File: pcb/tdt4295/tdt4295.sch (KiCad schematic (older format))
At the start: 0 parts

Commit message: simple efm connections
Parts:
- added C?: 1uF, symbol Device:C
- added C? (x2): 12pF, symbol Device:C
- added C?: 4.7uF, symbol Device:C
- added J?: MCU Debug Header, symbol Connector_Generic:Conn_02x10_Odd_Even
- added U?: EFM32GG12B810F1024GQ64, efm32gg-footprint:EFM32GG12B810F1024GQ64, symbol EFM32GG12B810F1024GQ64:EFM32GG12B810F1024GQ64
- added Y?: 48MHz, symbol Device:Crystal_GND24
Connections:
- net labels added: +1V0, +1V8, +3V3, +3V3A, +5V, 48MHZ_P1, 48MHZ_P3, GND, USB_D+, USB_D-
- wire segments 0 -> 88
- no-connect marks 0 -> 6
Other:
- note added: "Vent med å bruke noen av pinnene til QSPI/USART.\nKommer an på hvilke drivere som finnes til EFM-en\nog hva som er enklest i FPGA"

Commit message: Finish labeling/connecting EFM32 pins
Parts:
- added J?: MCU GPIO Header, symbol Connector_Generic:Conn_02x10_Odd_Even
- added J?: SD_Card, symbol Connector:SD_Card
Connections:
- net labels added: DBG_SWCLK, DBG_SWDIO, DBG_SWO, GPIO_PA12, GPIO_PA8, GPIO_PB11, GPIO_PB12, GPIO_PB8, GPIO_PD0, GPIO_PD1, GPIO_PD2, GPIO_PD3, GPIO_PD5, GPIO_PD6, GPIO_PD8, GPIO_PE7, GPIO_PF12, GPIO_PF5, MCU_RESETN, QSPI0_CS0, QSPI0_CS1, QSPI0_DQ0, QSPI0_DQ1, QSPI0_DQ2, QSPI0_DQ3, QSPI0_DQ4, QSPI0_DQ5, QSPI0_DQ6, QSPI0_DQ7, QSPI0_DQS, QSPI0_SCLK, SDIO_CD, SDIO_CLK, SDIO_CMD, SDIO_DAT0, SDIO_DAT1, SDIO_DAT2, SDIO_DAT3, SDIO_WP, US3_CLK, US3_CS, US3_CTS, US3_RTS, US3_RX, US3_TX
- wire segments 88 -> 174
- no-connect marks 6 -> 9
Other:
- note added: "EFM32GG MCU"
- note added: "VREGI/VBUS/VREGO\nAlle knyttet til 5V-regulator\nIkke egt. nødvendig"
- note removed: "Vent med å bruke noen av pinnene til QSPI/USART.\nKommer an på hvilke drivere som finnes til EFM-en\nog hva som er enklest i FPGA"
- moved on the sheet: C?, J?, U?, Y?

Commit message: rework some efm wiring according to application notes
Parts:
- removed C?: 4.7uF, symbol Device:C
- added C? (x5): 0.1uF, symbol Device:C
- added C? (x3): 10uF, symbol Device:C
- added C?: 10nF, symbol Device:C
- added C?: 1uF, symbol Device:C
- added R? (x2): 15, symbol Device:R
- J?: value MCU Debug Header -> ARM 20 Pin Debug Header
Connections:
- wire segments 174 -> 206
- no-connect marks 9 -> 10
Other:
- note added: "AN0046\n2.2"
- note added: "RESETn has internal pullup"
- note added: "See AN0002.1\nFig 3.3"
- note added: "VREGI has\ninternal p.down"
- note removed: "VREGI/VBUS/VREGO\nAlle knyttet til 5V-regulator\nIkke egt. nødvendig"
- moved on the sheet: C?, J?, Y?

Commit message: remove analog 3v3 output
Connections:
- net labels removed: +3V3A
- wire segments 206 -> 204
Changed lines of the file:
@@
 F2 "USB_D+" B R 1900 1050 50
 F3 "USB_D-" B R 1900 1150 50
-F4 "+5V" O R 1900 1450 50
-F5 "+3V3" O R 1900 1550 50
-F6 "+3V3A" O R 1900 1650 50
-F7 "+1V8" O R 1900 1750 50
-F8 "+1V0" O R 1900 1850 50
+F4 "+5V" O R 1900 1550 50
+F5 "+3V3" O R 1900 1650 50
+F6 "+1V8" O R 1900 1750 50
+F7 "+1V0" O R 1900 1850 50
 $EndSheet
 $Comp
@@
 L power:+5V #PWR?
 U 1 1 61455354
-P 2000 1400
-F 0 "#PWR?" H 2000 1250 50  0001 C CNN
-F 1 "+5V" H 2015 1573 50  0000 C CNN
-F 2 "" H 2000 1400 50  0001 C CNN
-F 3 "" H 2000 1400 50  0001 C CNN
-	1    2000 1400
+P 2000 1500
+F 0 "#PWR?" H 2000 1350 50  0001 C CNN
+F 1 "+5V" H 2015 1673 50  0000 C CNN
+F 2 "" H 2000 1500 50  0001 C CNN
+F 3 "" H 2000 1500 50  0001 C CNN
+	1    2000 1500
 	1    0    0    -1
 $EndComp
 Wire Wire Line
-	2000 1400 2000 1450
+	2000 1500 2000 1550
 Wire Wire Line
-	2000 1450 1900 1450
+	2000 1550 1900 1550
 $Comp
 L power:+3V3 #PWR?
 U 1 1 61455D75
-P 2200 1400
-F 0 "#PWR?" H 2200 1250 50  0001 C CNN
-F 1 "+3V3" H 2215 1573 50  0000 C CNN
-F 2 "" H 2200 1400 50  0001 C CNN
-F 3 "" H 2200 1400 50  0001 C CNN
-	1    2200 1400
-	1    0    0    -1
-$EndComp
-$Comp
-L tdt4295:+3V3A #PWR?
-U 1 1 614565B9
-P 2450 1400
-F 0 "#PWR?" H 2450 1250 50  0001 C CNN
-F 1 "+3V3A" H 2465 1573 50  0000 C CNN
-F 2 "" H 2450 1400 50  0001 C CNN
-F 3 "" H 2450 1400 50  0001 C CNN
-	1    2450 1400
+P 2200 1500
+F 0 "#PWR?" H 2200 1350 50  0001 C CNN
+F 1 "+3V3" H 2215 1673 50  0000 C CNN
+F 2 "" H 2200 1500 50  0001 C CNN
+F 3 "" H 2200 1500 50  0001 C CNN
+	1    2200 1500
 	1    0    0    -1
 $EndComp
@@
 L power:+1V8 #PWR?
 U 1 1 61456C3B
-P 2700 1400
-F 0 "#PWR?" H 2700 1250 50  0001 C CNN
-F 1 "+1V8" H 2715 1573 50  0000 C CNN
-F 2 "" H 2700 1400 50  0001 C CNN
-F 3 "" H 2700 1400 50  0001 C CNN
-	1    2700 1400
+P 2450 1500
+F 0 "#PWR?" H 2450 1350 50  0001 C CNN
+F 1 "+1V8" H 2465 1673 50  0000 C CNN
+F 2 "" H 2450 1500 50  0001 C CNN
+F 3 "" H 2450 1500 50  0001 C CNN
+	1    2450 1500
 	1    0    0    -1
 $EndComp
@@
 L power:+1V0 #PWR?
 U 1 1 614570F0
-P 2950 1400
-F 0 "#PWR?" H 2950 1250 50  0001 C CNN
-F 1 "+1V0" H 2965 1573 50  0000 C CNN
-F 2 "" H 2950 1400 50  0001 C CNN
-F 3 "" H 2950 1400 50  0001 C CNN
-	1    2950 1400
+P 2700 1500
+F 0 "#PWR?" H 2700 1350 50  0001 C CNN
+F 1 "+1V0" H 2715 1673 50  0000 C CNN
+F 2 "" H 2700 1500 50  0001 C CNN
+F 3 "" H 2700 1500 50  0001 C CNN
+	1    2700 1500
 	1    0    0    -1
 $EndComp
 Wire Wire Line
-	1900 1550 2200 1550
+	1900 1650 2200 1650
 Wire Wire Line
-	2200 1550 2200 1400
+	2200 1650 2200 1500
 Wire Wire Line
-	2450 1400 2450 1650
+	1900 1750 2450 1750
 Wire Wire Line
-	2450 1650 1900 1650
+	2450 1750 2450 1500
 Wire Wire Line
-	1900 1750 2700 1750
+	2700 1500 2700 1850
 Wire Wire Line
-	2700 1750 2700 1400
-Wire Wire Line
-	2950 1400 2950 1850
-Wire Wire Line
-	2950 1850 1900 1850
+	2700 1850 1900 1850
 $Comp
 L power:GND #PWR?

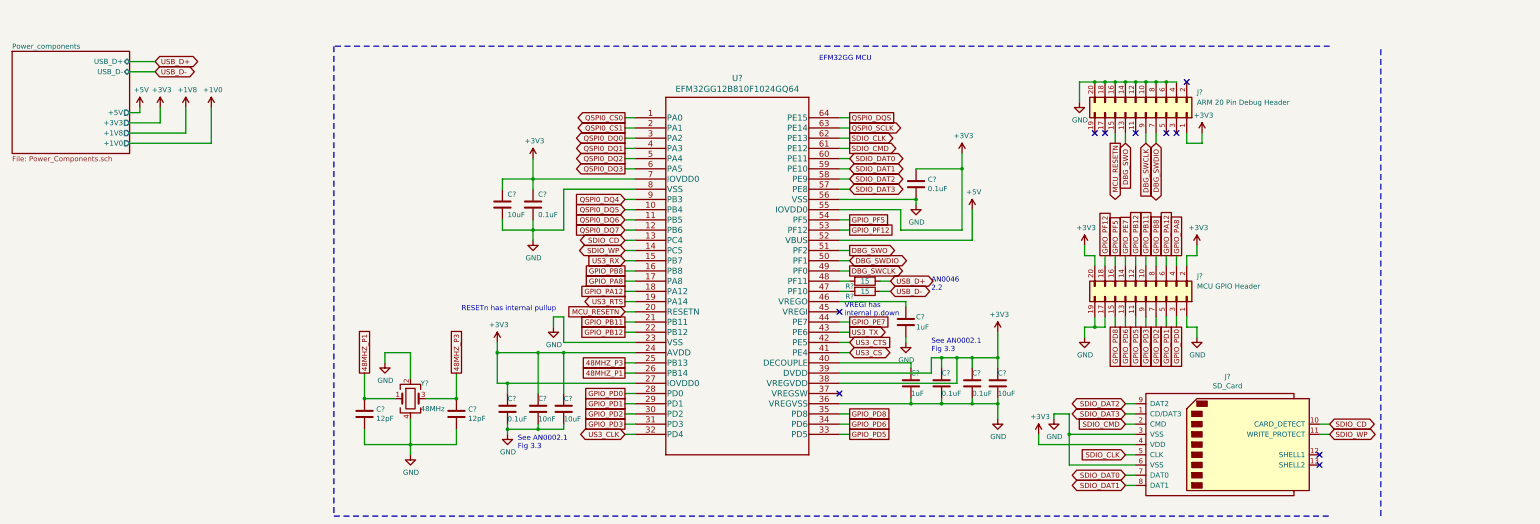
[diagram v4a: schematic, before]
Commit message: rework power regulator to only use tps54294
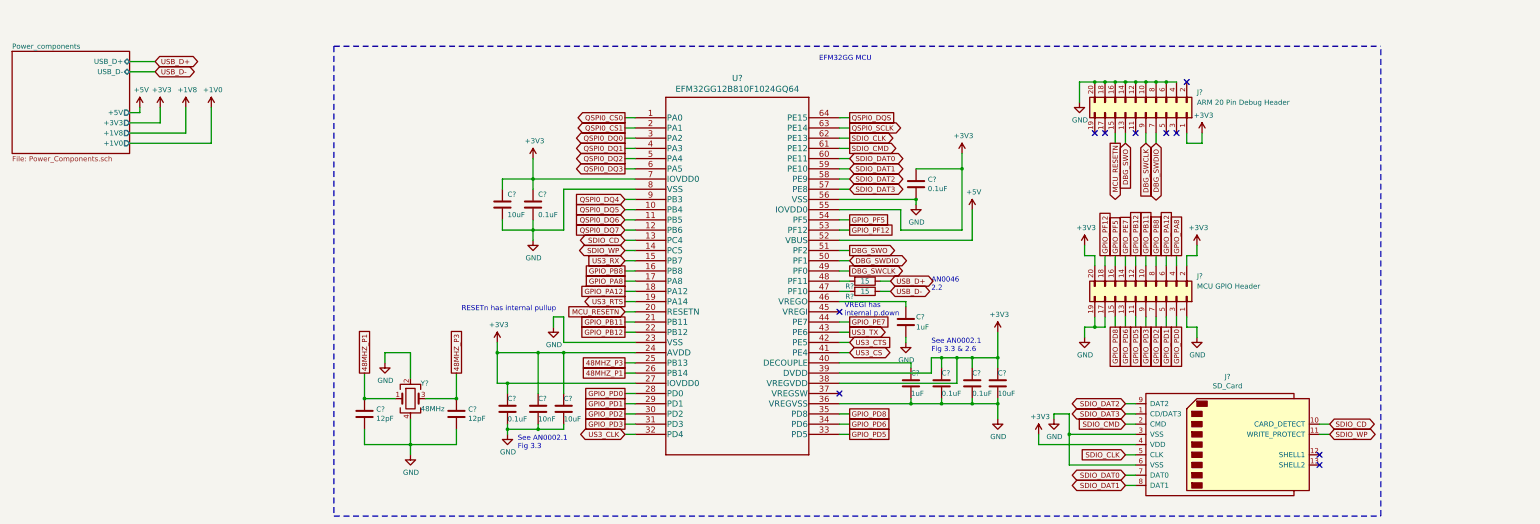
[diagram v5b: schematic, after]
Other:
- note added: "See AN0002.1\nFig 3.3 & 2.6"
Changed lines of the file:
@@
 Wire Notes Line
 	14150 5500 14150 900
-Wire Notes Line
-	13650 900  3900 900
 Text Notes 8650 1050 0    50   ~ 0
 EFM32GG MCU
@@
 Wire Wire Line
 	13550 4700 13650 4700
-Wire Notes Line
-	3900 5500 13650 5500
 Wire Notes Line
 	3900 900  3900 5500
@@
 	9550 4400 9850 4400
 Text Notes 9750 3900 0    50   ~ 0
-See AN0002.1\nFig 3.3
+See AN0002.1\nFig 3.3 & 2.6
 Text Notes 5700 4850 0    50   ~ 0
 See AN0002.1\nFig 3.3
@@
 Wire Wire Line
 	9500 3400 8850 3400
+Wire Notes Line
+	3900 5500 14150 5500
+Wire Notes Line
+	3900 900  14150 900
 $EndSCHEMATC

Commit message: Add pushbuttons & LEDs to EFM32GG GPIO ports
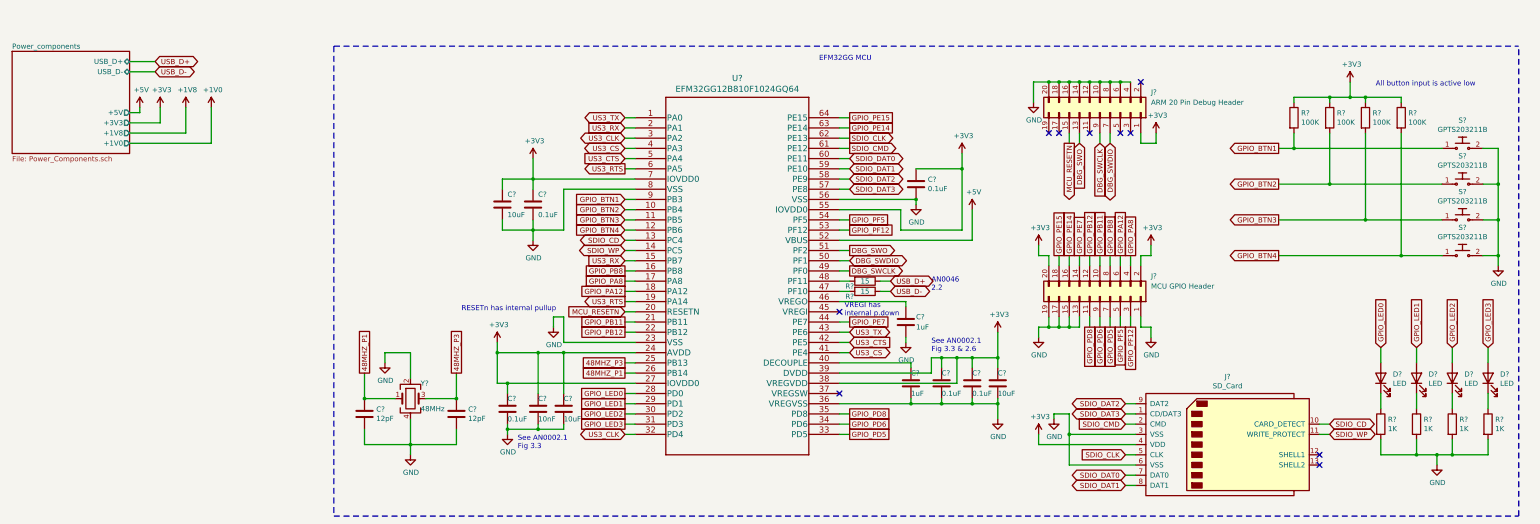
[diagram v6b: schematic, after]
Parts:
- added D? (x4): LED, symbol Device:LED
- added R? (x4): 100K, symbol Device:R
- added R? (x4): 1K, symbol Device:R
- added S? (x4): GPTS203211B, digikey-footprints:PushButton_12x12mm_THT_GPTS203211B, symbol dk_Pushbutton-Switches:GPTS203211B
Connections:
- net QSPI0_CS0 is gone; now on net US3_TX: U?.1 (PA0)
- net QSPI0_CS1 is gone; now on net US3_RX: U?.2 (PA1)
- net QSPI0_DQ0 is gone; now on net US3_CLK: U?.3 (PA2)
- net QSPI0_DQ1 is gone; now on net US3_CS: U?.4 (PA3)
- net QSPI0_DQ2 is gone; now on net US3_CTS: U?.5 (PA4)
- net QSPI0_DQ3 is gone; now on net US3_RTS: U?.6 (PA5)
- net +3V3: now also R?.1, R?.1, R?.1, R?.1
- net GND: now also J?.13 (Pin_13), J?.15 (Pin_15), R?.2, R?.2, R?.2, R?.2, S?.2, S?.2, S?.2, S?.2
- net GPIO_PD5: now also J?.7 (Pin_7); no longer J?.11 (Pin_11)
- net GPIO_PD6: now also J?.9 (Pin_9); no longer J?.13 (Pin_13)
- net GPIO_PD8: now also J?.11 (Pin_11); no longer J?.15 (Pin_15)
- net GPIO_PF12: now also J?.3 (Pin_3); no longer J?.18 (Pin_18)
- net GPIO_PF5: now also J?.5 (Pin_5); no longer J?.16 (Pin_16)
- net GPIO_PD0 renamed GPIO_LED0
- net GPIO_LED0: now also D?.2 (A); no longer J?.3 (Pin_3)
- net GPIO_PD1 renamed GPIO_LED1
- net GPIO_LED1: now also D?.2 (A); no longer J?.5 (Pin_5)
- net GPIO_PD2 renamed GPIO_LED2
- net GPIO_LED2: now also D?.2 (A); no longer J?.7 (Pin_7)
- net GPIO_PD3 renamed GPIO_LED3
- net GPIO_LED3: now also D?.2 (A); no longer J?.9 (Pin_9)
- net QSPI0_DQ4 renamed GPIO_BTN1
- net GPIO_BTN1: now also R?.2, S?.1
- net QSPI0_DQ5 renamed GPIO_BTN2
- net GPIO_BTN2: now also R?.2, S?.1
- net QSPI0_DQ6 renamed GPIO_BTN3
- net GPIO_BTN3: now also R?.2, S?.1
- net QSPI0_DQ7 renamed GPIO_BTN4
- net GPIO_BTN4: now also R?.2, S?.1
- net QSPI0_DQS renamed GPIO_PE15
- net GPIO_PE15: now also J?.18 (Pin_18)
- net QSPI0_SCLK renamed GPIO_PE14
- net GPIO_PE14: now also J?.16 (Pin_16)
- new net: D?.1 (K), R?.1 (x4)
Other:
- note added: "All button input is active low"
- moved on the sheet: J?

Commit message: rework MCU pinning
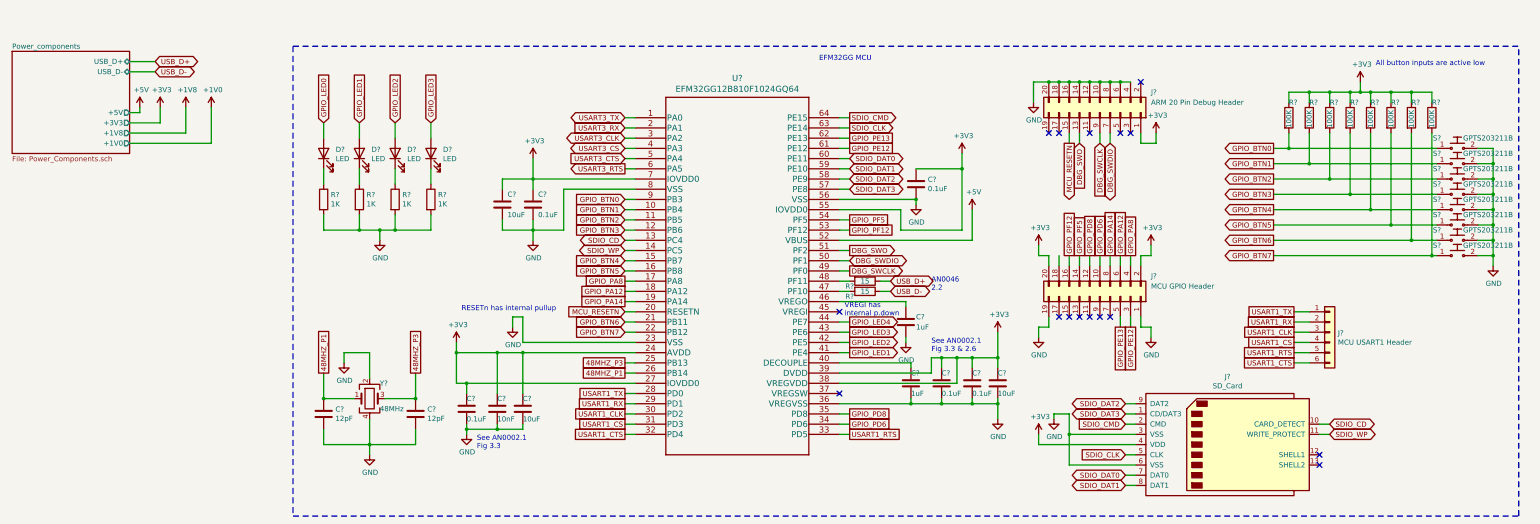
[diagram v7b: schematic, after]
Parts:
- added J?: MCU USART1 Header, symbol Connector_Generic:Conn_01x06
- added R? (x4): 100K, symbol Device:R
- added S? (x4): GPTS203211B, digikey-footprints:PushButton_12x12mm_THT_GPTS203211B, symbol dk_Pushbutton-Switches:GPTS203211B
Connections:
- net +3V3: now also R?.1, R?.1, R?.1, R?.1
- net GND: now also S?.2, S?.2, S?.2, S?.2; no longer J?.13 (Pin_13), J?.15 (Pin_15), J?.17 (Pin_17)
- net GPIO_BTN1: now also R?.2, S?.1, U?.10 (PB4); no longer R?.2, S?.1, U?.9 (PB3)
- net GPIO_BTN2: now also R?.2, S?.1, U?.11 (PB5); no longer R?.2, S?.1, U?.10 (PB4)
- net GPIO_BTN3: now also R?.2, S?.1, U?.12 (PB6); no longer R?.2, S?.1, U?.11 (PB5)
- net GPIO_BTN4: now also U?.15 (PB7), R?.2, S?.1; no longer R?.2, S?.1, U?.12 (PB6)
- net GPIO_LED0: no longer U?.28 (PD0)
- net GPIO_LED1: now also U?.41 (PE4); no longer U?.29 (PD1)
- net GPIO_LED2: now also U?.42 (PE5); no longer U?.30 (PD2)
- net GPIO_LED3: now also U?.43 (PE6); no longer U?.31 (PD3)
- net GPIO_PD6: now also J?.10 (Pin_10); no longer J?.9 (Pin_9)
- net GPIO_PD8: now also J?.12 (Pin_12); no longer J?.11 (Pin_11)
- net GPIO_PF12: now also J?.16 (Pin_16); no longer J?.3 (Pin_3)
- net GPIO_PF5: now also J?.14 (Pin_14); no longer J?.5 (Pin_5)
- net SDIO_CLK: now also U?.63 (PE14); no longer U?.62 (PE13)
- net SDIO_CMD: now also U?.64 (PE15); no longer U?.61 (PE12)
- net GPIO_PB11 renamed GPIO_BTN6
- net GPIO_BTN6: now also R?.2, S?.1; no longer J?.10 (Pin_10)
- net GPIO_PB12 renamed GPIO_BTN7
- net GPIO_BTN7: now also R?.2, S?.1; no longer J?.12 (Pin_12)
- net GPIO_PB8 renamed GPIO_BTN5
- net GPIO_BTN5: now also R?.2, S?.1; no longer J?.8 (Pin_8)
- net GPIO_PD5: no longer names the net of J?.7 (Pin_7)
- net GPIO_PD5: no longer U?.33 (PD5)
- removed net GPIO_PE14: J?.16 (Pin_16), U?.63 (PE14)
- net GPIO_PE15: no longer names the net of J?.18 (Pin_18)
- net GPIO_PE15: no longer U?.64 (PE15)
- net GPIO_PE7 renamed GPIO_LED4
- net GPIO_LED4: no longer J?.14 (Pin_14)
- net US3_CLK renamed USART1_CTS
- net USART1_CTS: now also J?.6 (Pin_6); no longer U?.3 (PA2)
- net US3_CS renamed USART3_CS
- net USART3_CS: no longer U?.41 (PE4)
- net US3_CTS renamed USART3_CTS
- net USART3_CTS: no longer U?.42 (PE5)
- net US3_RTS renamed GPIO_PA14
- net GPIO_PA14: now also J?.8 (Pin_8); no longer U?.6 (PA5)
- net US3_RX renamed USART3_RX
- net USART3_RX: no longer U?.15 (PB7)
- net US3_TX renamed USART3_TX
- net USART3_TX: no longer U?.43 (PE6)
- new net GPIO_BTN0: R?.2, S?.1, U?.9 (PB3)
- new net GPIO_PE12: J?.3 (Pin_3), U?.61 (PE12)
- new net GPIO_PE13: J?.5 (Pin_5), U?.62 (PE13)
- new net USART1_CLK: J?.3 (Pin_3), U?.30 (PD2)
- new net USART1_CS: J?.4 (Pin_4), U?.31 (PD3)
- new net USART1_RTS: J?.5 (Pin_5), U?.33 (PD5)
- new net USART1_RX: J?.2 (Pin_2), U?.29 (PD1)
- new net USART1_TX: J?.1 (Pin_1), U?.28 (PD0)
- new net USART3_CLK: U?.3 (PA2)
- new net USART3_RTS: U?.6 (PA5)
- no-connect marks 10 -> 16
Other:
- note added: "All button inputs are active low"
- note removed: "All button input is active low"
- moved on the sheet: C?, D?, R?, S?, Y?

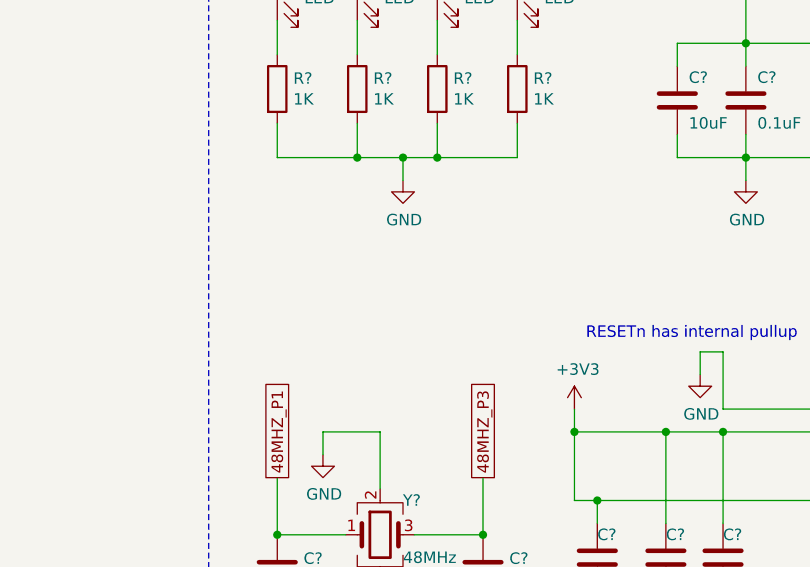
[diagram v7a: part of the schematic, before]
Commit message: 3v3 decouplers
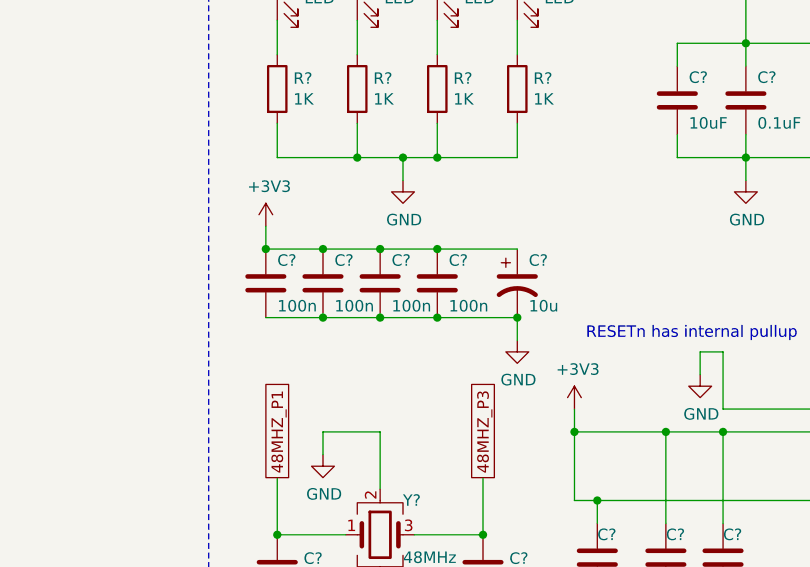
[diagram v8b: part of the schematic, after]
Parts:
- added C? (x4): 100n, symbol Device:C
- added C?: 10u, symbol Device:CP1
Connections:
- net +3V3: now also C?.1, C?.1, C?.1, C?.1, C?.1
- net GND: now also C?.2, C?.2, C?.2, C?.2, C?.2
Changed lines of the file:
@@
 Wire Wire Line
 	13450 4000 13300 4000
+$Comp
+L power:+3V3 #PWR?
+U 1 1 61D12730
+P 3750 3000
+F 0 "#PWR?" H 3750 2850 50  0001 C CNN
+F 1 "+3V3" H 3765 3173 50  0000 C CNN
+F 2 "" H 3750 3000 50  0001 C CNN
+F 3 "" H 3750 3000 50  0001 C CNN
+	1    3750 3000
+	1    0    0    -1
+$EndComp
+$Comp
+L Device:C C?
+U 1 1 61D13A02
+P 3750 3250
+F 0 "C?" H 3800 3350 50  0000 L CNN
+F 1 "100n" H 3800 3150 50  0000 L CNN
+F 2 "" H 3788 3100 50  0001 C CNN
+F 3 "~" H 3750 3250 50  0001 C CNN
+	1    3750 3250
+	1    0    0    -1
+$EndComp
+$Comp
+L Device:C C?
+U 1 1 61D1453C
+P 4000 3250
+F 0 "C?" H 4050 3350 50  0000 L CNN
+F 1 "100n" H 4050 3150 50  0000 L CNN
+F 2 "" H 4038 3100 50  0001 C CNN
+F 3 "~" H 4000 3250 50  0001 C CNN
+	1    4000 3250
+	1    0    0    -1
+$EndComp
+$Comp
+L Device:C C?
+U 1 1 61D14932
+P 4250 3250
+F 0 "C?" H 4300 3350 50  0000 L CNN
+F 1 "100n" H 4300 3150 50  0000 L CNN
+F 2 "" H 4288 3100 50  0001 C CNN
+F 3 "~" H 4250 3250 50  0001 C CNN
+	1    4250 3250
+	1    0    0    -1
+$EndComp
+$Comp
+L Device:C C?
+U 1 1 61D14CA7
+P 4500 3250
+F 0 "C?" H 4550 3350 50  0000 L CNN
+F 1 "100n" H 4550 3150 50  0000 L CNN
+F 2 "" H 4538 3100 50  0001 C CNN
+F 3 "~" H 4500 3250 50  0001 C CNN
+	1    4500 3250
+	1    0    0    -1
+$EndComp
+$Comp
+L Device:CP1 C?
+U 1 1 61D15B12
+P 4850 3250
+F 0 "C?" H 4900 3350 50  0000 L CNN
+F 1 "10u" H 4900 3150 50  0000 L CNN
+F 2 "" H 4850 3250 50  0001 C CNN
+F 3 "~" H 4850 3250 50  0001 C CNN
+	1    4850 3250
+	1    0    0    -1
+$EndComp
+Wire Wire Line
+	4850 3100 4500 3100
+Wire Wire Line
+	4500 3100 4250 3100
+Connection ~ 4500 3100
+Wire Wire Line
+	4250 3100 4000 3100
+Connection ~ 4250 3100
+Wire Wire Line
+	4000 3100 3750 3100
+Connection ~ 4000 3100
+Wire Wire Line
+	3750 3100 3750 3000
+Connection ~ 3750 3100
+Wire Wire Line
+	3750 3400 4000 3400
+Wire Wire Line
+	4000 3400 4250 3400
+Connection ~ 4000 3400
+Wire Wire Line
+	4250 3400 4500 3400
+Connection ~ 4250 3400
+Wire Wire Line
+	4500 3400 4850 3400
+Connection ~ 4500 3400
+$Comp
+L power:GND #PWR?
+U 1 1 61DC8D46
+P 4850 3500
+F 0 "#PWR?" H 4850 3250 50  0001 C CNN
+F 1 "GND" H 4855 3327 50  0000 C CNN
+F 2 "" H 4850 3500 50  0001 C CNN
+F 3 "" H 4850 3500 50  0001 C CNN
+	1    4850 3500
+	1    0    0    -1
+$EndComp
+Wire Wire Line
+	4850 3500 4850 3400
+Connection ~ 4850 3400
 $EndSCHEMATC
